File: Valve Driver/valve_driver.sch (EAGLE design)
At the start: 15 parts

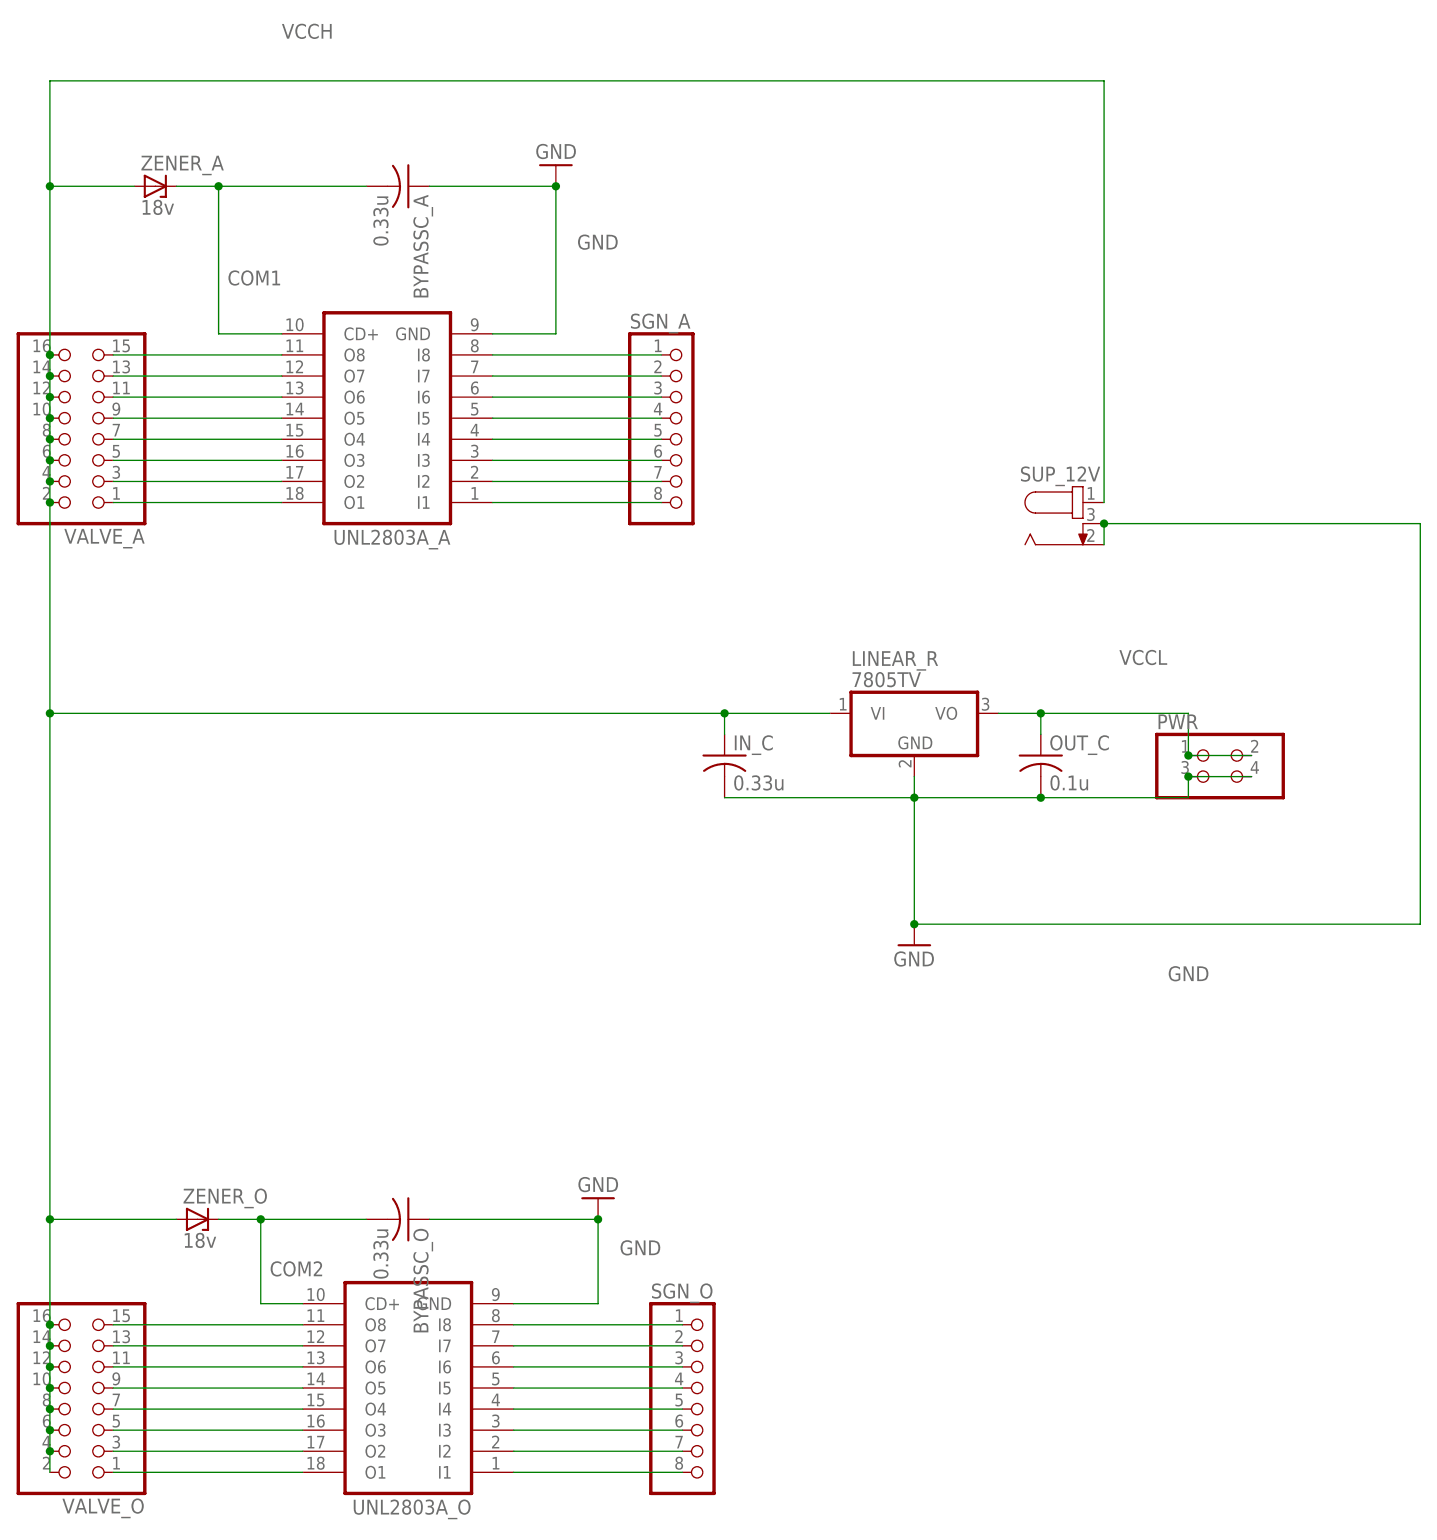
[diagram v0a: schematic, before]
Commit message: Revert "20180712-change-pin"
This reverts commit fb38f18733497d936434fddb3c409504ab7d6048.
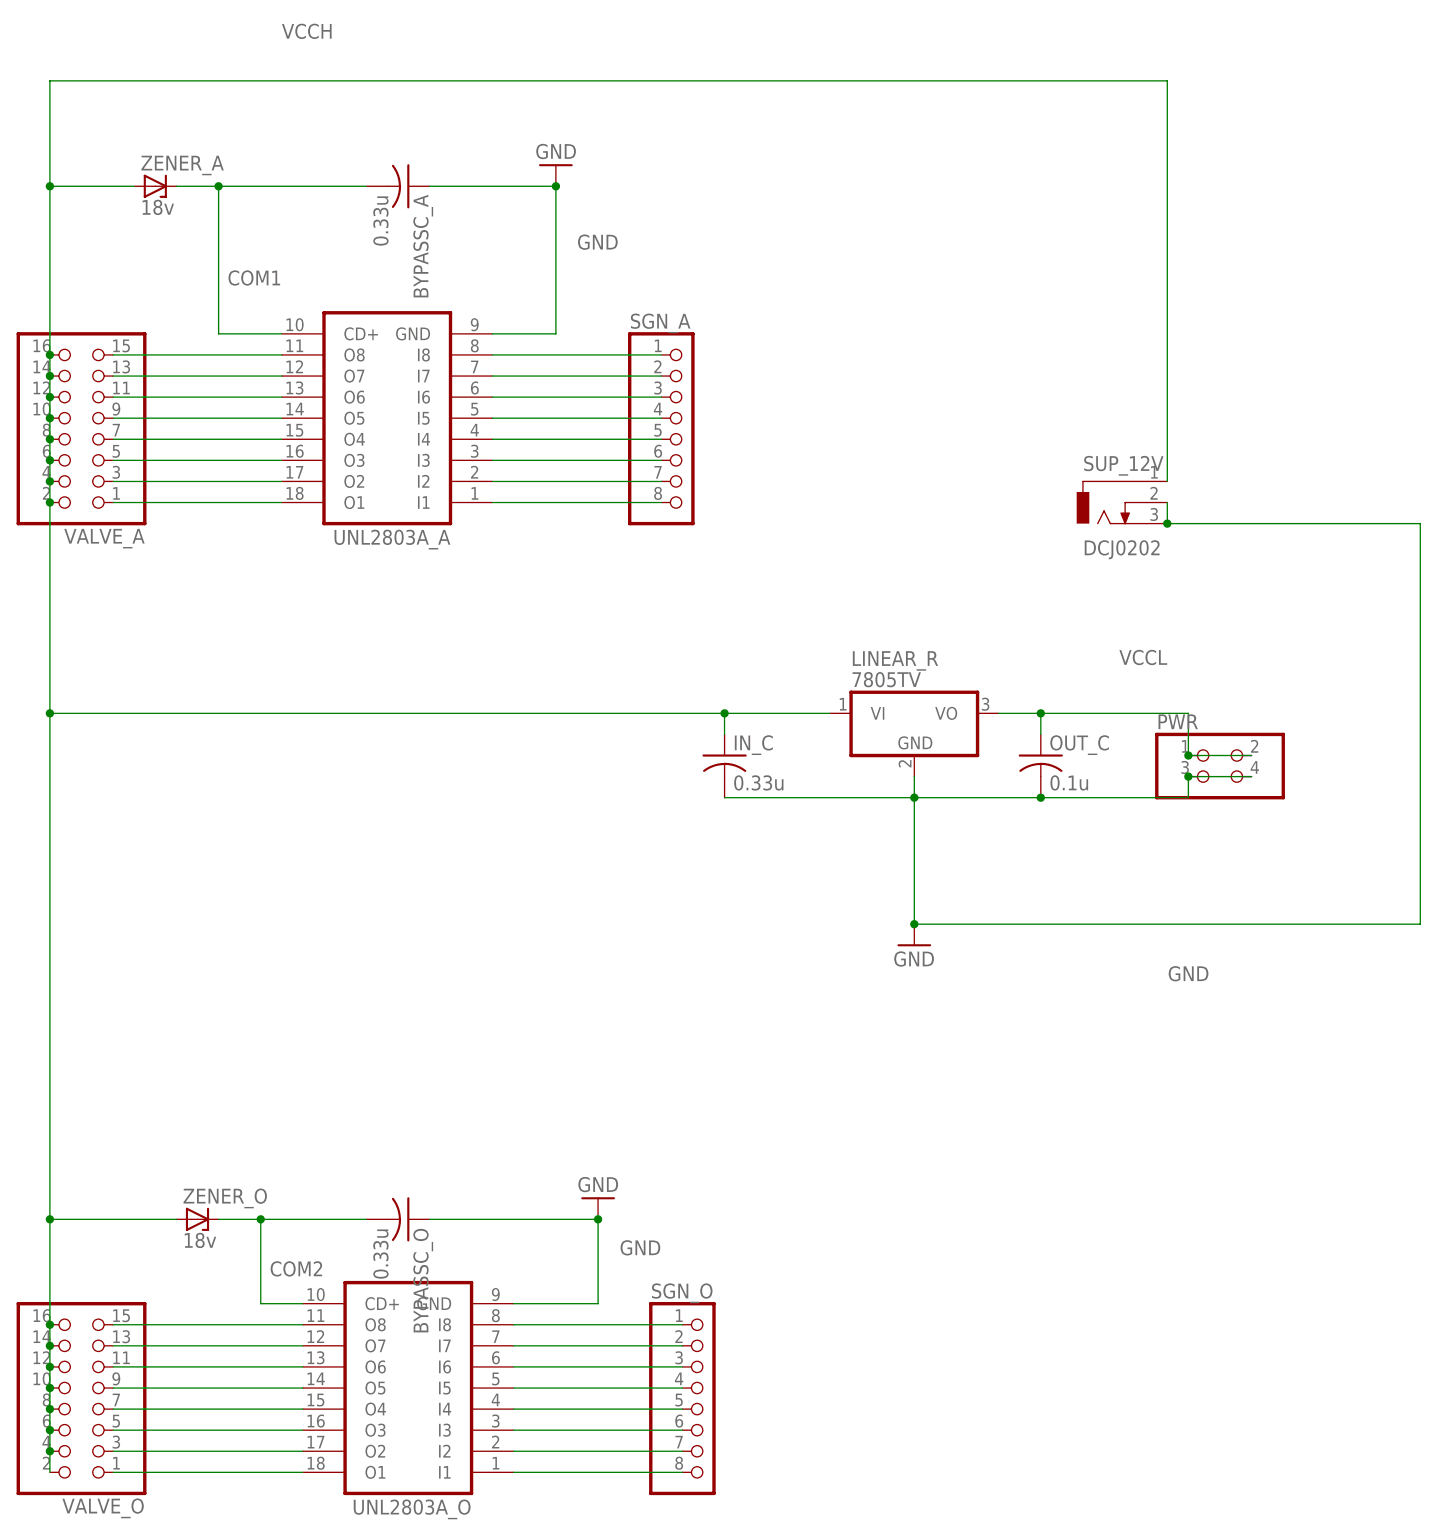
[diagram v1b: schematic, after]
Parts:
- SUP_12V: value (none) -> DCJ0202; device mylib:694108301002 -> con-jack:DCJ0202
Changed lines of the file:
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@@
 <attribute name="OC_NEWARK" value="unknown"/>
 </part>
-<part name="SUP_12V" library="mylib" deviceset="694108301002" device="" package3d_urn="urn:adsk.eagle:package:3359594/1"/>
+<part name="SUP_12V" library="con-jack" library_urn="urn:adsk.eagle:library:154" deviceset="DCJ0202" device="" package3d_urn="urn:adsk.eagle:package:7491/1"/>
 <part name="VALVE_A" library="pinhead" library_urn="urn:adsk.eagle:library:325" deviceset="PINHD-2X8" device="" package3d_urn="urn:adsk.eagle:package:22481/2"/>
 <part name="VALVE_O" library="pinhead" library_urn="urn:adsk.eagle:library:325" deviceset="PINHD-2X8" device="" package3d_urn="urn:adsk.eagle:package:22481/2"/>
@@
 <wire x1="205.74" y1="134.62" x2="205.74" y2="182.88" width="0.1524" layer="91"/>
 <pinref part="SUP_12V" gate="G$1" pin="3"/>
-<wire x1="205.74" y1="182.88" x2="167.64" y2="182.88" width="0.1524" layer="91"/>
+<wire x1="205.74" y1="182.88" x2="175.26" y2="182.88" width="0.1524" layer="91"/>
 <pinref part="SUP_12V" gate="G$1" pin="2"/>
-<wire x1="167.64" y1="180.34" x2="167.64" y2="182.88" width="0.1524" layer="91"/>
-<junction x="167.64" y="182.88"/>
+<wire x1="175.26" y1="185.42" x2="175.26" y2="182.88" width="0.1524" layer="91"/>
+<junction x="175.26" y="182.88"/>
 <pinref part="GND1" gate="1" pin="GND"/>
 <junction x="144.78" y="134.62"/>
@@
 <pinref part="ZENER_A" gate="1" pin="A"/>
 <pinref part="SUP_12V" gate="G$1" pin="1"/>
-<wire x1="167.64" y1="185.42" x2="167.64" y2="236.22" width="0.1524" layer="91"/>
-<wire x1="167.64" y1="236.22" x2="40.64" y2="236.22" width="0.1524" layer="91"/>
+<wire x1="175.26" y1="187.96" x2="175.26" y2="236.22" width="0.1524" layer="91"/>
+<wire x1="175.26" y1="236.22" x2="40.64" y2="236.22" width="0.1524" layer="91"/>
 <wire x1="40.64" y1="236.22" x2="40.64" y2="223.52" width="0.1524" layer="91"/>
 <wire x1="40.64" y1="223.52" x2="50.8" y2="223.52" width="0.1524" layer="91"/>
